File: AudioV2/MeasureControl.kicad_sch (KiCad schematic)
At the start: 104 parts, among them J1601 AUDIO, J1602 V_IN, J1603 15_V_IN, SW1601 DEST sense (3PDT 3rd pole, sa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, U1601 OPA1656, U1602 OPA1656, U1603 LT1763-3.3, U1604 MBC2596-01, U1605 TPS3307-33, U1606 LT1763-5, U1607 BP5293-50, U1608 OPA1656, U1609 XC8107AC20MR-G, U1610 MCP23017 (UI 0x22), Y1601 ASFL1-12.288MHZ-EC-T

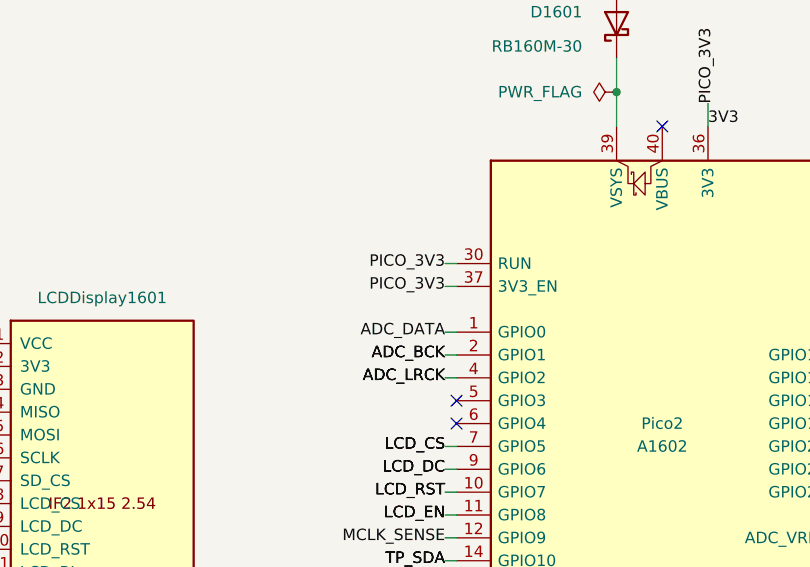
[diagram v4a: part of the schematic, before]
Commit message: AudioV2: Pico の 3V3_EN を開放に戻した（3.3V が立ち上がらない恐れ）
A1602(Pico2) の pin 37 3V3_EN が、Pico 自身の 3V3 出力(pin 36)と同じ
ネットに載っていた。3V3_EN はオンボード SMPS のイネーブル入力で、
Pico 内部で 100k でしか VSYS に吊られていない。それを自分が作る側の
レールに繋いでいたので、起動前は 100k と 3V3 側 DC 負荷の分圧になる。

DEST ラダーの R1656 + R1657 = 20k が SW 位置に関係なく常時 3V3 と
D_GND の間に載っているため:

  起動前の 3V3_EN ~= VSYS 4.6V x 20k/(100k+20k) ~= 0.77V

EN しきい値がこれより高ければ SMPS は起動せず、3.3V 系（MCP23017 x3、
OLED、I2C プルアップ、娘基板スロット両方）が丸ごと立たない。低ければ
起動してラッチする。どちらに転ぶかは Pico 2 データシートに EN しきい値の
記載が無く確定できない。意図して作る回路ではないので開放に戻す。

Pico 2 データシート:
  「3V3_EN connects to the on-board SMPS enable pin, and is pulled high
   (to VSYS) via a 100k resistor. To disable the 3.3V ... short this pin low」
→ 通常動作は開放が正。AGENT_HANDOFF.md にも「RUN・3V3_EN は no_connect」と
  記録があり、AGND(33)・VBUS(40) には実際に付いている。

pin 37 のスタブ配線(1.27mm)と PICO_3V3 ラベルを外し、ピン先に no_connect を
立てた。pin 30 RUN と pin 35 ADC_VREF はそれぞれ独立したスタブで、今回は
触っていない（RUN は内部 50k プルアップがあり電気的に等価、ADC_VREF は
DS が 3V3 との短絡を明示的に想定しているため急がない）。

検証:
  A1602.37    3V3 -> 未接続
  3V3 ネット  28 -> 27 ピン
  erc         17 件（変化なし）
  netlist     部品 369 / 重複 0（変化なし）
  check_sexpr 13 ファイル / 問題 0
  roundtrip   OK

指摘は sch-review エージェント。回路図と一次資料で裏を取ってから適用した。

Co-Authored-By: Claude Opus 5 <noreply@anthropic.com>
Claude-Session: https://claude.ai/code/session_01VCArLcCGbMGgxvWJ5HFJiY
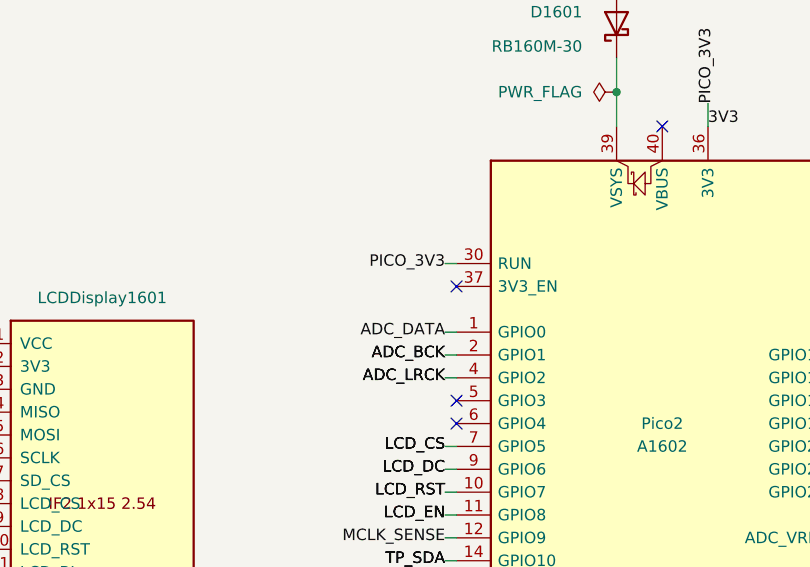
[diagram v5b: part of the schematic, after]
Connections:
- net 3V3: no longer A1602.37 (3V3_EN)
- no-connect marks 24 -> 25
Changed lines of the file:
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@@
-	(wire
-		(pts
-			(xy 247.65 147.32) (xy 248.92 147.32)
-		)
-		(stroke
-			(width 0)
-			(type default)
-		)
-	)
 	(wire
 		(pts
@@
 	(label "ADC_nMR"
 		(at 247.65 190.5 180)
-		(effects
-			(font
-				(size 1.27 1.27)
-			)
-			(justify right)
-		)
-	)
-	(label "PICO_3V3"
-		(at 247.65 147.32 180)
 		(effects
 			(font
@@
 		)
 	)
+	(no_connect
+		(at 248.92 147.32)
+	)
 	(symbol

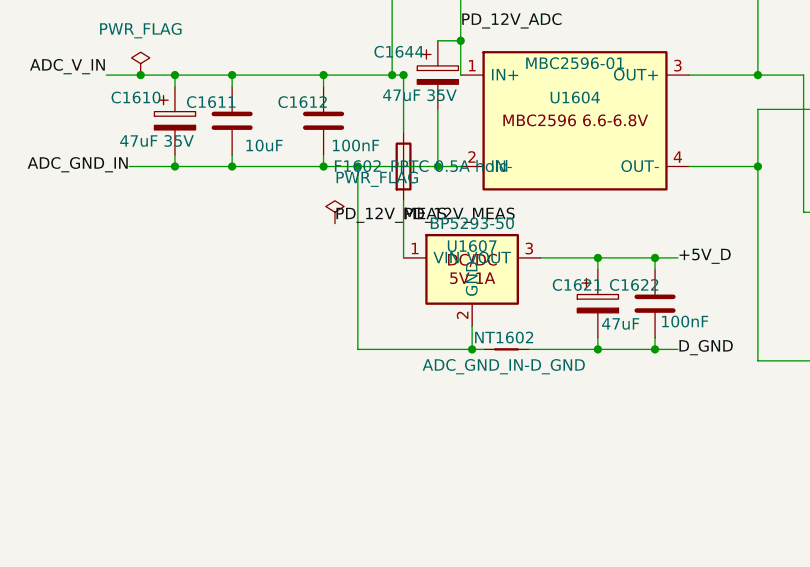
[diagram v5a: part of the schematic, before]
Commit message: AudioV2: U1607(+5V_D) の出力ループを局所で閉じた
査読（接地・ノイズ）の指摘。U1607(BP5293-50) は GND ピンが PD_GND なのに、
出力コンデンサ3個（C1621 47u / C1622 100n / C1633 10u）も負荷（D1601→Pico
VSYS、U1609 LCD負荷SW）も D_GND にあった。出力電流が全部 D_GND へ落ち、
NT1602 1本で PD_GND へ戻っていた。NT1602 が「静かな基準の1点結合」ではなく
電源の帰線になっていた。

同じ設計の U403（リレー用 BP5293）が手本になっている。あちらは GND=GND_COIL
で出力コンデンサも GND_COIL、負荷も GND_COIL で、出力ループが娘基板内で閉じる。
原則は「コンバータの GND は、負荷が帰るグランドに置く」。

  U1607.2 GND   PD_GND -> D_GND
  C1645 10uF 50V  PD_12V_MEAS <-> D_GND  （新規。入力コンデンサ）

**⚠ 入力コンデンサの帰り先は D_GND であって PD_GND ではない。**
査読が挙げた案は PD_GND だったが、それでは目的を達しない。降圧コンバータで
脈流なのは入力側で、GND を D_GND に移したあと入力Cを PD_GND に落とすと、
脈流ループが NT1602 を通ってしまい逆に悪化する。D_GND に落とせば入力ループが
U1607 の直近で閉じ、NT1602 を通るのは平均電流だけになる。
BP5293 の DS p.2「入力コンデンサは不要だが特性を良くするならセラミック 10uF
推奨」、p.19 図29「負荷急変で入力電圧が落ちて出力が不安定なら Ci を足す」。

MeasureControl は手編集所有。U1607.2 は縦スタブ1本で PD_GND 網に繋がって
いただけなので、そのワイヤと、意味を失うジャンクション（3本が集まっていた点が
同一直線の2本になる）を外し、ピン先に D_GND ラベルを置いた。PD_GND 網の
他の4ピン（NT1602.1 / C1610.2 / C1611.2 / C1612.2）は触っていない。

検証:
  U1607.2     PD_GND -> D_GND
  PD_GND      13 -> 12 ピン
  PD_12V_MEAS 2 -> 3 ピン（C1645.1 が載った）
  erc         17 件（変化なし・新規違反なし）
  netlist     部品 370 / 重複 0（369 + C1645）
  dangling    0 本 / 暗黙接触 0 件
  check_sexpr 13 ファイル / 問題 0
  roundtrip   OK

CLAUDE.md の期待値表も 370 に更新した。

なお同じ査読の「PT2314E の帰路が2系統に割れている」は論理構成の問題として
保留（ユーザー判断）。実物で pin2-pin25 の導通を当たれば分岐が決まる。

Co-Authored-By: Claude Opus 5 <noreply@anthropic.com>
Claude-Session: https://claude.ai/code/session_01VCArLcCGbMGgxvWJ5HFJiY
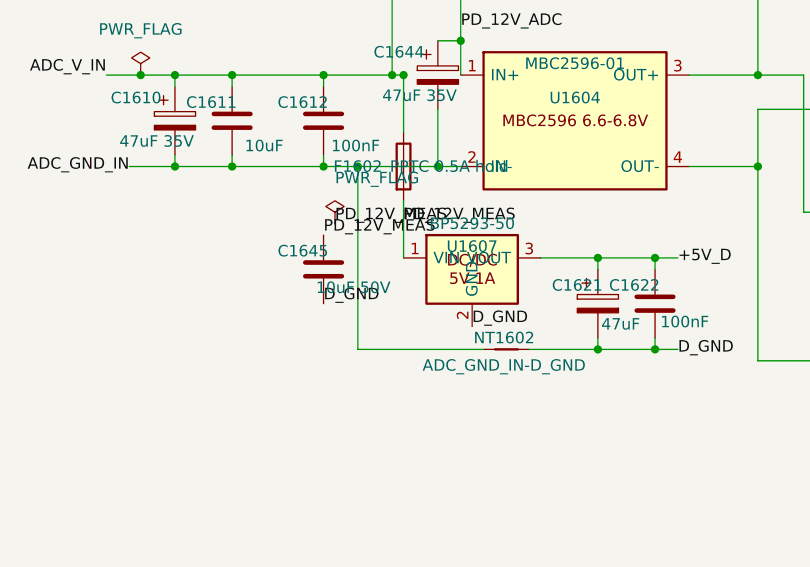
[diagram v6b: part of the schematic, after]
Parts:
- added C1645: 10uF 50V, Capacitor_SMD:C_1206_3216Metric_Pad1.33x1.80mm_HandSolder, symbol Device:C
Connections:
- net ADC_GND_IN: no longer U1607.2 (GND)
- net D_GND: now also U1607.2 (GND), C1645.2
- net PD_12V_MEAS: now also C1645.1
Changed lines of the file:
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@@
 	)
 	(junction
-		(at 270.51 74.93)
-		(diameter 0)
-		(color 0 0 0 0)
-	)
-	(junction
 		(at 318.77 76.2)
 		(diameter 0)
@@
 	(wire
 		(pts
-			(xy 270.51 72.39) (xy 270.51 74.93)
-		)
-		(stroke
-			(width 0)
-			(type default)
-		)
-	)
-	(wire
-		(pts
 			(xy 30.48 200.66) (xy 34.29 200.66)
 		)
@@
 		)
 	)
+	(label "D_GND"
+		(at 270.51 72.39 0)
+		(effects
+			(font
+				(size 1.27 1.27)
+			)
+			(justify left bottom)
+		)
+	)
+	(symbol
+		(lib_id "Device:C")
+		(at 254 66.04 0)
+		(unit 1)
+		(body_style 1)
+		(exclude_from_sim no)
+		(in_bom yes)
+		(on_board yes)
+		(in_pos_files yes)
+		(dnp no)
+		(property "Reference" "C1645"
+			(at 251.714 64.008 0)
+			(show_name no)
+			(do_not_autoplace no)
+			(effects
+				(font
+					(size 1.27 1.27)
+				)
+			)
+		)
+		(property "Value" "10uF 50V"
+			(at 257.302 68.072 0)
+			(show_name no)
+			(do_not_autoplace no)
+			(effects
+				(font
+					(size 1.27 1.27)
+				)
+			)
+		)
+		(property "Footprint" "Capacitor_SMD:C_1206_3216Metric_Pad1.33x1.80mm_HandSolder"
+			(at 254 66.04 0)
+			(hide yes)
+			(show_name no)
+			(do_not_autoplace no)
+			(effects
+				(font
+					(size 1.27 1.27)
+				)
+			)
+		)
+		(property "Datasheet" ""
+			(at 254 66.04 0)
+			(hide yes)
+			(show_name no)
+			(do_not_autoplace no)
+			(effects
+				(font
+					(size 1.27 1.27)
+				)
+			)
+		)
+		(property "Description" "U1607(BP5293-50) の入力コンデンサ CIN。DS p.2 推奨 10uF。帰り先は D_GND（U1607 の GND と同じ）。PD_GND に落とすと入力の脈流ループが NT1602 を通ってしまう。"
+			(at 254 66.04 0)
+			(hide yes)
+			(show_name no)
+			(do_not_autoplace no)
+			(effects
+				(font
+					(size 1.27 1.27)
+				)
+			)
+		)
+		(pin "1"
+		)
+		(pin "2"
+		)
+		(instances
+			(project "AudioV2Case"
+				(path "/a1000001-0001-4001-8001-000000000001/a1000012-0012-4012-8012-000000000012/43e41fda-fe26-43e3-950a-c017f3070bbf"
+					(reference "C1645")
+					(unit 1)
+				)
+			)
+		)
+	)
+	(label "PD_12V_MEAS"
+		(at 254 62.23 0)
+		(effects
+			(font
+				(size 1.27 1.27)
+			)
+			(justify left bottom)
+		)
+	)
+	(label "D_GND"
+		(at 254 69.85 0)
+		(effects
+			(font
+				(size 1.27 1.27)
+			)
+			(justify left bottom)
+		)
+	)

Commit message: AudioV2: パネル部品6個をヘッダのフットプリントにした（16 -> 10）
PARTS.md がヘッダ構成まで既に指定していた。それに従っただけで、新しい判断は
入れていない。

  PARTS.md:5    RV / SW_DEST / ENC / PWR SW は パネル実装。基板はヘッダ＋リード
  PARTS.md:173  RV は基板 6P ヘッダ（Device:R_Potentiometer_Dual ピン番号のまま）
  PARTS.md:141  SW_DEST は 現物端子 -> 基板ヘッダ（音声 2x4 + センス 1x3）

  RV501/502     PinHeader_1x06   シンボルのピン 1-6 がそのままヘッダのピン
  SW501/502     PinHeader_1x04   PARTS.md §2.1 の SW601-1..4 / SW602-1..4 に対応
  SW1601        PinHeader_1x04   同じ並び。pin2(MUTE) は基板側で未使用
  SW402         PinHeader_1x02   SPST

ポットの品種（Alps RK27 か RK097 か Alpha RD901 か）は決めていない。
PARTS.md が「RK097 でも回路は同一」「A50k デュアルならピン互換で可」と
書いており、電気的な要件は A カーブ・50k・2連だけ。**ヘッダなので基板側は
品種に依存しない**。入手性と性能で選ぶ調達判断として残す（ユーザー判断 2026-09-07）。

⚠ PARTS.md の「音声 2x4」は 2行4列ではなく「4ピンを2組」と読んだ。同 §2.1 の
ピン対応表が SW601-1..4 / SW602-1..4 と別々に並べており、シンボルも2つに
分かれているため。2行4列の1個を意図していたなら要修正。

副次的に、Cursor 査読の「DEST の 3PDT が自動 BOM 上で現物3個に見える」も解ける。
基板に載るのはヘッダ3個（実際に3個要る）で、スイッチ本体はパネル部品として
基板 BOM に出ないのが正しい形。

なお PARTS.md §2.1 のピン対応表は SW601-3 をコモン（AMP_SEL_L）としており、
今日 SW1601 で直した割り当て（pin3=コモン）と一致していた。

検証:
  未設定      16 -> 10（残りは D403・F201/202/203・J201/202・J_HP501・
              J_LINE501・J_RAIL501・U202。すべて調達判断待ち）
  netlist     部品 370 / 重複 0（変化なし）
  erc         17 件（変化なし）
  check_sexpr 13 ファイル / 問題 0
  roundtrip   6/6 OK
  再生成      2回目でバイト一致

Co-Authored-By: Claude Opus 5 <noreply@anthropic.com>
Claude-Session: https://claude.ai/code/session_01VCArLcCGbMGgxvWJ5HFJiY
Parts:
- SW1601: footprint (none) -> Connector_PinHeader_2.54mm:PinHeader_1x04_P2.54mm_Vertical
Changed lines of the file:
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@@
 			)
 		)
-		(property "Footprint" ""
+		(property "Footprint" "Connector_PinHeader_2.54mm:PinHeader_1x04_P2.54mm_Vertical"
 			(at 0 0 0)
 			(hide yes)

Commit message: AudioV2: 外部入力端子台を入れ、ENC の名前と UI の割り込みを直した（ERC 17 -> 11）
査読の確認で出た3件。ERC は 17 -> 11 件になり、残る11件は全部「宣言済みの型」に
収まった（内訳は CLAUDE.md の表）。

1. 外部入力 L/R の端子台 J_IN401 を追加

   DECISIONS §11.3（基板間リンク）は「外部入力 L/R｜端子台 2〜3P」で確定と
   書いてあるのに symbol が無く、COMMON_L / COMMON_R が1ピン（結合Cの片足だけ）
   だった。出力側は J_HP501 / J_LINE501 が実在するのに入力だけ抜けていた。
   このまま PCB を起こすと入力パッドが空かない。

       J_IN401 → COMMON_L →C406→ PT_LIN → PT2314E → PT_OUT_L →C405→ TONE_L → …

   1=L / 2=A_GND / 3=R。L と R の間に必ず GND が挟まる並び。フットプリントは
   J_RAIL501 と同じ Phoenix MKDS-1,5 3P（横）。
   これで isolated_pin_label が 9 -> 1 件になった（残る1件は DEST_SENSE_MUTE_NC で、
   ミュート位置なので意図的に開放）。

2. ENC1602 の Value を ENC_VOL -> ENC_BASS

   確定は CH / BASS / TREBLE（DECISIONS §2「ENC 割当（確定）」・§10 の表・
   CIRCUIT_DESIGN.md）。「音量をエンコーダー化」は 2026-08-30 に撤回済み。
   そもそも PT2314E のボリューム段は LOUT/ROUT -> LIN/RIN のインサートで
   飛ばしているので、VOL のエンコーダには制御対象が無い。

3. U1610（UI 0x22）の INTA(20) / INTB(19) を Pico の GP16 / GP17 へ

   エンコーダ3個が MCP23017 経由なので、割り込みが無いとポーリングしかない。
   I²C は PT2314E の VDD 9V（L7809CV）× MCU 3.3V により Standard 100 kbit/s 止まり
   （DS p.7 の DATA RATE 表）で、2.42″ OLED が 128x64 なら1フレーム 1024 バイト
   ≈ 92 ms。取りこぼさない周期でエンコーダを叩くとバス占有が単独で 45% になり
   同居できない。

   ⚠ 2本引いたのは MIRROR ビット頼みにしないため。ENC1/2 の A/B/SW と ENC3 の A/B は
     PortA(21-28) だが ENC3_SW だけ PortB(pin1) にいるので、INTA だけだと
     IOCON.MIRROR=1 が前提になる。ADC 兼用の GP26-28 は空けたまま。

Pico の AGND(33) は開放のまま戻した（いったん D_GND へ結んだが撤回）

   lib シンボル MCU_Module:RaspberryPi_Pico は pin3 GND と pin33 AGND を
   どちらも power_out と型付けしている（他の GND 6本は passive）。モジュール側が
   それぞれをグランド源として出しているという宣言なので、外で結ぶと power_out
   同士の衝突になり、実際 pin_to_pin エラーが出た。AGND は Pico 基板上で
   グランドに繋がっている前提でよい。

PARTS.md は再生成した（gen_parts_bom.py）

   生成ブロックが 部品総数 368 / Footprint 未設定 44 の時代のまま止まっていたので、
   このセッションで埋めた footprint 全部と R401 / C1645 / F1603 / J_IN401、
   削除した R407・R412-415 が一気に反映された。
   ⚠ U402 の Role にあった「SOP-28 300 mil。LCSC C90034」は 2fbad17 で
     生成ブロックの中を手編集していたもので、再生成で消えた（マーカー内は毎回
     まるごと差し替わるので当然）。回路図側の Description プロパティに入れ直した。
   §5 の「Footprint 未設定の部品」は 0 個になったので残件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
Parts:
- ENC1602: value ENC_VOL -> ENC_BASS
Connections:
- net ENC_INTA: now reaches A1602.21 (GPIO16)
- net ENC_INTA: now also U1610.20 (INTA)
- net ENC_INTB: now reaches A1602.22 (GPIO17)
- net ENC_INTB: now also U1610.19 (INTB)
- no-connect marks 25 -> 21
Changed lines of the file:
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@@
 	)
 	(no_connect
-		(at 106.68 337.82)
-	)
-	(no_connect
 		(at 294.64 170.18)
 	)
@@
 	)
 	(no_connect
-		(at 294.64 190.5)
-	)
-	(no_connect
 		(at 132.08 360.68)
 	)
@@
 	)
 	(no_connect
-		(at 106.68 335.28)
-	)
-	(no_connect
 		(at 132.08 353.06)
 	)
 	(no_connect
-		(at 294.64 154.94)
-	)
-	(no_connect
-		(at 294.64 157.48)
-	)
-	(no_connect
 		(at 194.31 168.91)
 	)
@@
 			)
 		)
-		(property "Value" "ENC_VOL"
+		(property "Value" "ENC_BASS"
 			(at 265.72 342.54 0)
 			(show_name no)
@@
 		)
 	)
+	(label "ENC_INTA"
+		(at 106.68 335.28 180)
+		(effects
+			(font
+				(size 1.27 1.27)
+			)
+			(justify right bottom)
+		)
+	)
+	(label "ENC_INTB"
+		(at 106.68 337.82 180)
+		(effects
+			(font
+				(size 1.27 1.27)
+			)
+			(justify right bottom)
+		)
+	)
+	(label "ENC_INTA"
+		(at 294.64 154.94 0)
+		(effects
+			(font
+				(size 1.27 1.27)
+			)
+			(justify left bottom)
+		)
+	)
+	(label "ENC_INTB"
+		(at 294.64 157.48 0)
+		(effects
+			(font
+				(size 1.27 1.27)
+			)
+			(justify left bottom)
+		)
+	)
+	(no_connect
+		(at 294.64 190.5)
+	)
 )
